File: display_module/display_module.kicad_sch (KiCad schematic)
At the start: 36 parts, among them J1 Conn_01x03_Female, J2 Conn_01x03_Male, J3 Conn_01x03_Female, J4 Conn_01x03_Male, J5 RESET, J6 HIGH, J7 PROG, J8 GND, SW1 PRIM, SW2 SEC, U1 74LS47, U2 74LS193, U3 MAN3410A, U4 74LS47, U5 74LS193, U6 MAN3410A

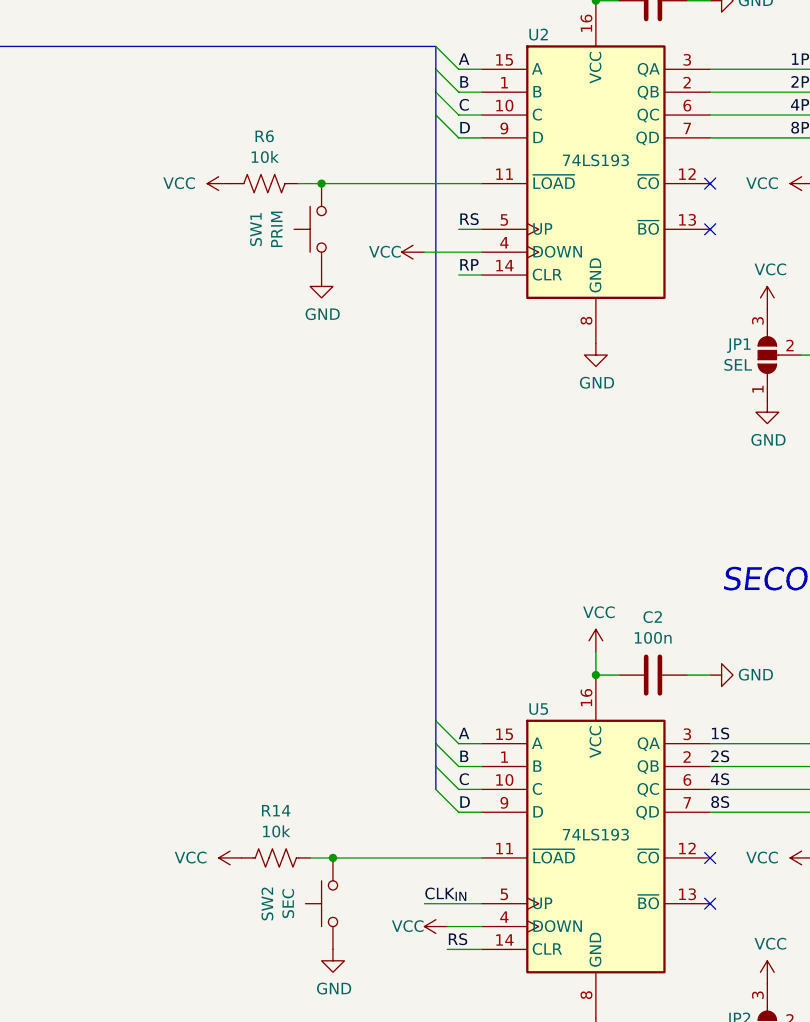
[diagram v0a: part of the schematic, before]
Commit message: New schematics and minor rev for display
Added a signal name to the display board for the data load signals for each counter.
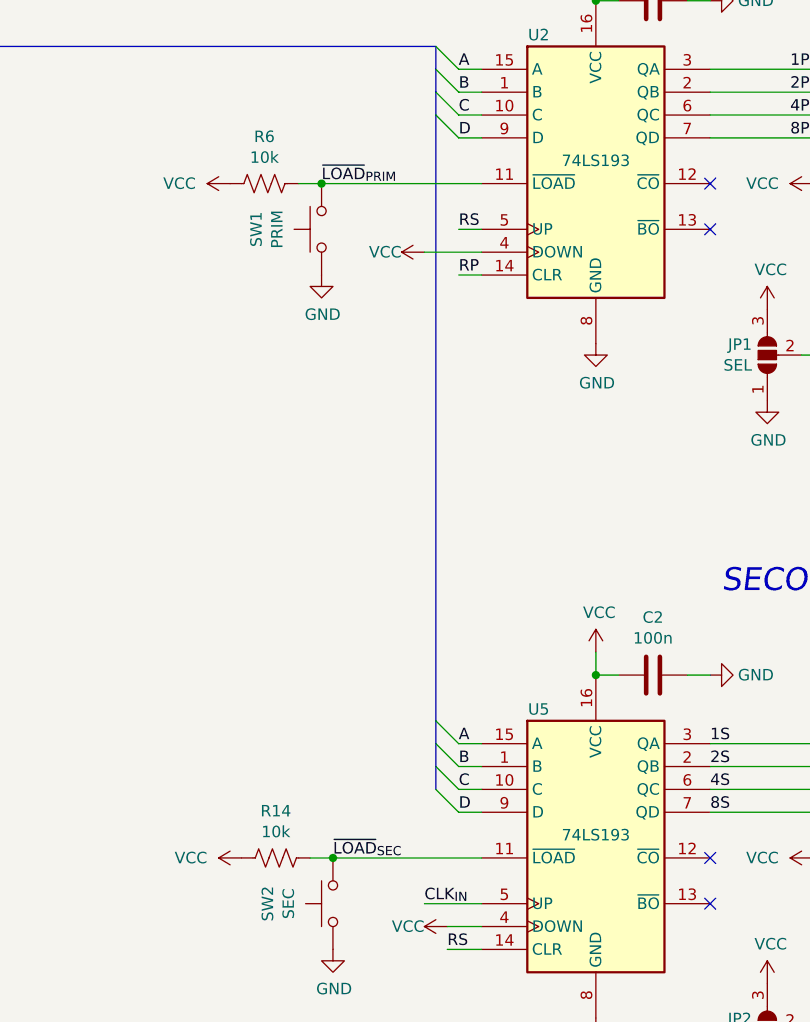
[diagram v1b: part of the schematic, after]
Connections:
- net ~{LOAD}_{SEC}: now reaches R14.1, SW2.2, U5.11 (~{LOAD})
- net ~{LOAD}_{PRIM}: now reaches R6.1, SW1.2, U2.11 (~{LOAD})
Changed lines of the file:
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@@
   (title_block
     (title "Clock Display Board")
-    (date "2021-11-28")
-    (rev "1")
+    (date "2022-03-25")
+    (rev "1.1")
     (company "Savo Bajic")
     (comment 2 "Can be used with CC displays by swapping U1/4 for CD4511s")
@@
     (effects (font (size 1.27 1.27)) (justify left bottom))
   )
+  (label "~{LOAD}_{PRIM}" (at 71.12 71.12 0)
+    (effects (font (size 1.27 1.27)) (justify left bottom))
+  )
   (label "A" (at 86.36 58.42 0)
     (effects (font (size 1.27 1.27)) (justify left bottom))
@@
     (effects (font (size 1.27 1.27)) (justify right bottom))
   )
+  (label "~{LOAD}_{SEC}" (at 72.39 146.05 0)
+    (effects (font (size 1.27 1.27)) (justify left bottom))
+  )
   (label "4S" (at 217.17 138.43 180)
